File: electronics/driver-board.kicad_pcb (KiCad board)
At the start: 2 copper layers, 40 x 40 mm, 54 parts, among them J1 Conn_01x02, J3 S4B-XH-A, J4 Qwiic_RA, J5 Conn_01x06_Female, SW1 SW_Push, SW2 SW_Push, SW3 SW_Push, SW4 SW_Push, U2 LMR16020PDDAR, U3 ESP32-C6-MINI-1/U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

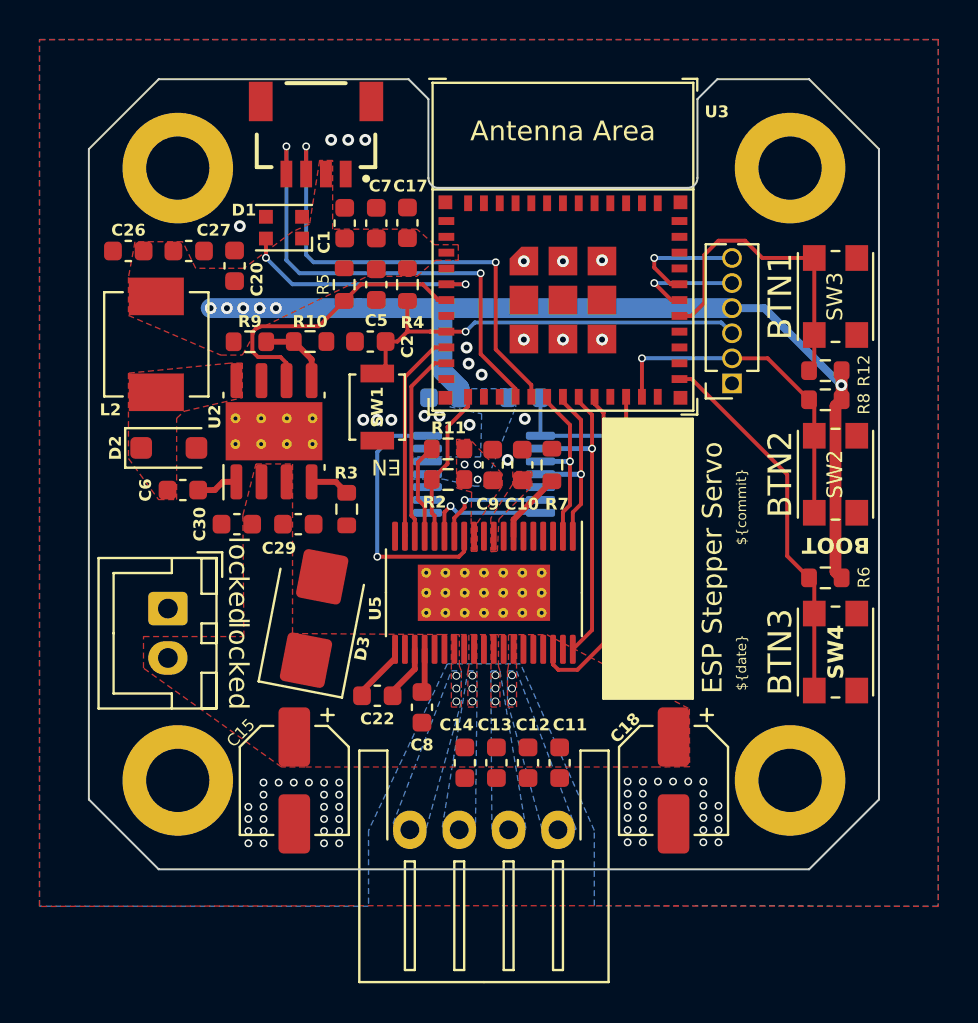
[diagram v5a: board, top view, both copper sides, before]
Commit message: moved a few traces to give space for ground path
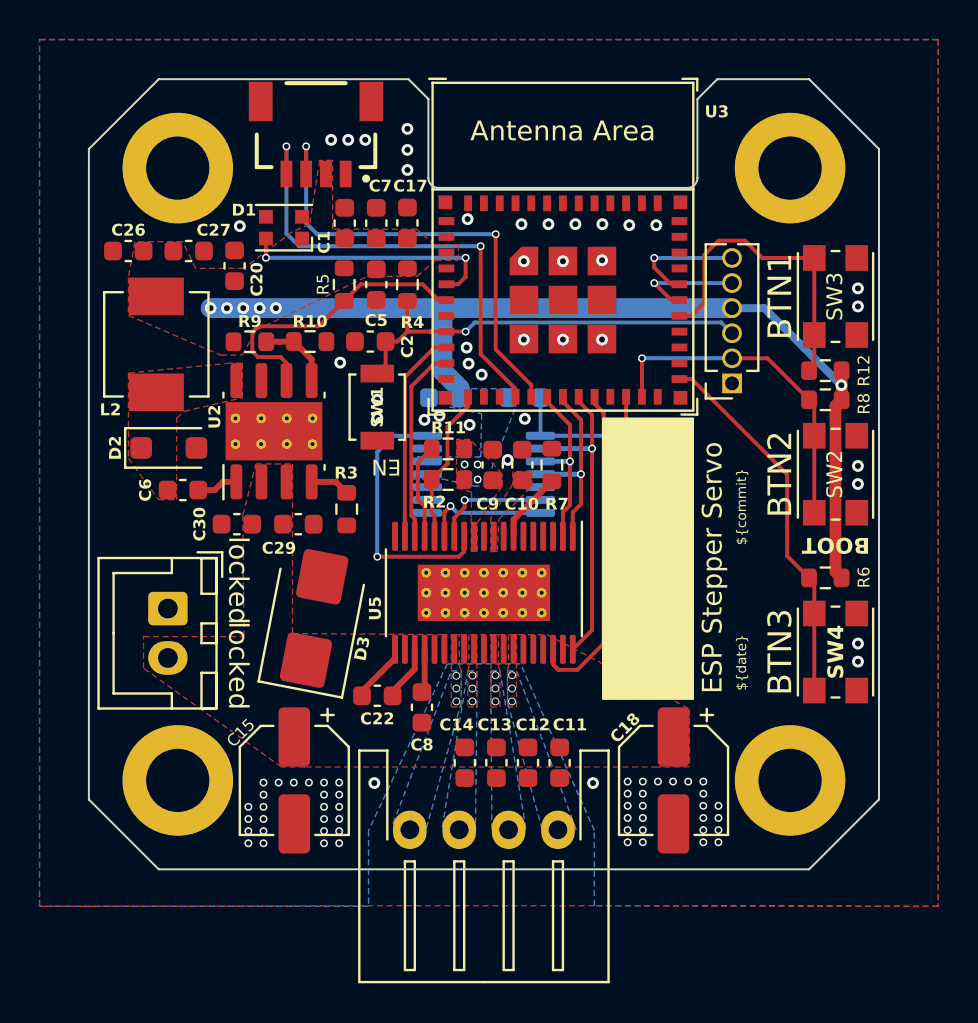
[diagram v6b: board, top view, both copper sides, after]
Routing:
- net Net-(D1-DIN): track 12.6 -> 13.2 mm
- net GND: vias 71 -> 89

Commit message: pull ups for i2c; teardrops on through hole connections
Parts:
- added R13: 10k, Resistor_SMD:R_0603_1608Metric, F.Cu at (39.0, 37.3)
- added R14: 10k, Resistor_SMD:R_0603_1608Metric, F.Cu at (40.7, 37.3)
- moved D1 3.09 mm to (40.2, 40.6), turned to 0 degrees
- moved C17 0.05 mm to (46.2, 37.3)
- moved R4 0.05 mm to (46.2, 40.4)
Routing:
- net /TMC_OUT1A: track 0.00 -> 8.23 mm
- net /TMC_OUT1B: track 0.00 -> 8.21 mm
- net /TMC_OUT2A: track 0.00 -> 7.86 mm
- net /TMC_OUT2B: track 0.00 -> 7.84 mm
- net Net-(D1-DIN): track 13.2 -> 9.53 mm
- net /I2C_SCL: track 24.3 -> 26.3 mm
- net /I2C_SDA: track 24.1 -> 25.9 mm
- net GND: track 0.00 -> 1.18 mm, vias 89 -> 90
- net +3V3: vias 9 -> 8
- removed copper zone on B.Cu, net /TMC_OUT1A
- removed copper zone on B.Cu, net /TMC_OUT1B
- removed copper zone on B.Cu, net /TMC_OUT2A
- removed copper zone on B.Cu, net /TMC_OUT2B

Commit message: fixed few connector part numbers
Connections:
- net Net-(U5-ENCA) renamed /ENCA
- net Net-(U5-ENCB) renamed /ENCB
- net Net-(U5-ENCN) renamed /ENCN
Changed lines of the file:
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@@
   (net 14 "unconnected-(U3-NC-Pad4)")
   (net 15 "unconnected-(U3-NC-Pad7)")
-  (net 16 "Net-(U5-ENCN)")
+  (net 16 "/ENCN")
   (net 17 "/TMC_DIAG0")
   (net 18 "unconnected-(U3-NC-Pad21)")
@@
   (net 40 "/SPI_SDI")
   (net 41 "/SPI_SDO")
-  (net 42 "Net-(U5-ENCB)")
-  (net 43 "Net-(U5-ENCA)")
+  (net 42 "/ENCB")
+  (net 43 "/ENCA")
   (net 44 "unconnected-(U5-REFL-Pad5)")
   (net 45 "unconnected-(U5-REFR-Pad6)")
@@
     (descr "JST XH series connector, B2B-XH-A (http://www.jst-mfg.com/product/pdf/eng/eXH.pdf), generated with kicad-footprint-generator")
     (tags "connector JST XH vertical")
-    (property "LCSC" "C3310225")
-    (property "Manf" "Wago")
-    (property "Manf#" "2060-472/998-404")
+    (property "LCSC" "C265283")
+    (property "Manf" "JST")
+    (property "Manf#" "B2B-XH-A-GU")
     (property "Sheetfile" "driver-board.kicad_sch")
     (property "Sheetname" "")
@@
   (footprint "SparkFun-Connector:JST04_1MM_RA" locked (layer "F.Cu")
     (at 41.5 34.8 180)
+    (property "LCSC" "C160404")
+    (property "Manf" "JST")
+    (property "Manf#" "SM04B-SRSS-TB")
     (property "PROD_ID" "CONN-13694")
     (property "Sheetfile" "driver-board.kicad_sch")
@@
       (net 2 "+3V3") (pinfunction "VCC_IO") (pintype "power_in"))
     (pad "12" smd roundrect locked (at -2.8625 1 270) (size 1.475 0.3) (layers "F.Cu" "F.Paste" "F.Mask") (roundrect_rratio 0.25)
-      (net 16 "Net-(U5-ENCN)") (pinfunction "ENCN") (pintype "input"))
+      (net 16 "/ENCN") (pinfunction "ENCN") (pintype "input"))
     (pad "13" smd roundrect locked (at -2.8625 1.5 270) (size 1.475 0.3) (layers "F.Cu" "F.Paste" "F.Mask") (roundrect_rratio 0.25)
-      (net 42 "Net-(U5-ENCB)") (pinfunction "ENCB") (pintype "input"))
+      (net 42 "/ENCB") (pinfunction "ENCB") (pintype "input"))
     (pad "14" smd roundrect locked (at -2.8625 2 270) (size 1.475 0.3) (layers "F.Cu" "F.Paste" "F.Mask") (roundrect_rratio 0.25)
-      (net 43 "Net-(U5-ENCA)") (pinfunction "ENCA") (pintype "input"))
+      (net 43 "/ENCA") (pinfunction "ENCA") (pintype "input"))
     (pad "15" smd roundrect locked (at -2.8625 2.5 270) (size 1.475 0.3) (layers "F.Cu" "F.Paste" "F.Mask") (roundrect_rratio 0.25)
       (net 29 "/TMC_ENABLE") (pinfunction "DRV_EN") (pintype "input"))
@@
       (net 1 "GND") (pinfunction "TST") (pintype "input"))
     (pad "6" smd roundrect locked (at -2.8625 -1.3 180) (size 1.475 0.4) (layers "B.Cu" "B.Paste" "B.Mask") (roundrect_rratio 0.25)
-      (net 42 "Net-(U5-ENCB)") (pinfunction "B") (pintype "output"))
+      (net 42 "/ENCB") (pinfunction "B") (pintype "output"))
     (pad "7" smd roundrect locked (at -2.8625 -1.95 180) (size 1.475 0.4) (layers "B.Cu" "B.Paste" "B.Mask") (roundrect_rratio 0.25)
-      (net 43 "Net-(U5-ENCA)") (pinfunction "A") (pintype "output"))
+      (net 43 "/ENCA") (pinfunction "A") (pintype "output"))
     (pad "8" smd roundrect locked (at 2.8625 -1.95 180) (size 1.475 0.4) (layers "B.Cu" "B.Paste" "B.Mask") (roundrect_rratio 0.25)
       (net 35 "unconnected-(U7-W{slash}PWM-Pad8)") (pinfunction "W/PWM") (pintype "output+no_connect"))
@@
       (net 1 "GND") (pinfunction "GND") (pintype "power_in"))
     (pad "14" smd roundrect locked (at 2.8625 1.95 180) (size 1.475 0.4) (layers "B.Cu" "B.Paste" "B.Mask") (roundrect_rratio 0.25)
-      (net 16 "Net-(U5-ENCN)") (pinfunction "I/PWM") (pintype "output"))
+      (net 16 "/ENCN") (pinfunction "I/PWM") (pintype "output"))
     (model "${KICAD6_3DMODEL_DIR}/Package_SO.3dshapes/TSSOP-14_4.4x5mm_P0.65mm.wrl"
       (offset (xyz 0 0 0))
@@
   (gr_line (start 56.394854 47.940251) (end 56.386652 47.932431)
     (stroke (width 0.1) (type solid)) (layer "F.SilkS"))
-  (gr_rect (start 56.037643 47.18656) (end 60.581203 61.358559)
-    (stroke (width 0.1) (type solid)) (fill solid) (layer "F.SilkS"))
   (gr_line (start 59.653498 58.952672) (end 59.650347 58.955913)
     (stroke (width 0.120011) (type solid)) (layer "F.SilkS"))
@@
   (gr_line (start 56.942106 58.273807) (end 56.94595 58.271504)
     (stroke (width 0.120011) (type solid)) (layer "F.SilkS"))
+  (gr_rect (start 60.581203 61.358559) (end 56.037643 47.18656)
+    (stroke (width 0.1) (type solid)) (fill solid) (layer "F.SilkS"))
   (gr_line (start 57.24924 57.213578) (end 57.247428 57.215286)
     (stroke (width 0.120011) (type solid)) (layer "F.SilkS"))
@@
     )
   )
-  (zone (net 42) (net_name "Net-(U5-ENCB)") (layer "F.Cu") (name "$teardrop_padvia$") (hatch edge 0.5)
+  (zone (net 42) (net_name "/ENCB") (layer "F.Cu") (name "$teardrop_padvia$") (hatch edge 0.5)
     (priority 30019)
     (attr (teardrop (type padvia)))
@@
     )
   )
-  (zone (net 16) (net_name "Net-(U5-ENCN)") (layer "F.Cu") (name "$teardrop_padvia$") (hatch edge 0.5)
+  (zone (net 16) (net_name "/ENCN") (layer "F.Cu") (name "$teardrop_padvia$") (hatch edge 0.5)
     (priority 30005)
     (attr (teardrop (type padvia)))
@@
     )
   )
-  (zone (net 43) (net_name "Net-(U5-ENCA)") (layer "F.Cu") (name "$teardrop_padvia$") (hatch edge 0.5)
+  (zone (net 43) (net_name "/ENCA") (layer "F.Cu") (name "$teardrop_padvia$") (hatch edge 0.5)
     (priority 30016)
     (attr (teardrop (type padvia)))
@@
     )
   )
-  (zone (net 16) (net_name "Net-(U5-ENCN)") (layer "B.Cu") (name "$teardrop_padvia$") (hatch edge 0.5)
+  (zone (net 16) (net_name "/ENCN") (layer "B.Cu") (name "$teardrop_padvia$") (hatch edge 0.5)
     (priority 30020)
     (attr (teardrop (type padvia)))
@@
     )
   )
-  (zone (net 42) (net_name "Net-(U5-ENCB)") (layer "B.Cu") (name "$teardrop_padvia$") (hatch edge 0.5)
+  (zone (net 42) (net_name "/ENCB") (layer "B.Cu") (name "$teardrop_padvia$") (hatch edge 0.5)
     (priority 30026)
     (attr (teardrop (type padvia)))
@@
     )
   )
-  (zone (net 43) (net_name "Net-(U5-ENCA)") (layer "B.Cu") (name "$teardrop_padvia$") (hatch edge 0.5)
+  (zone (net 43) (net_name "/ENCA") (layer "B.Cu") (name "$teardrop_padvia$") (hatch edge 0.5)
     (priority 30024)
     (attr (teardrop (type padvia)))
